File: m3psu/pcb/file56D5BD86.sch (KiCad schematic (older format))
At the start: 44 parts

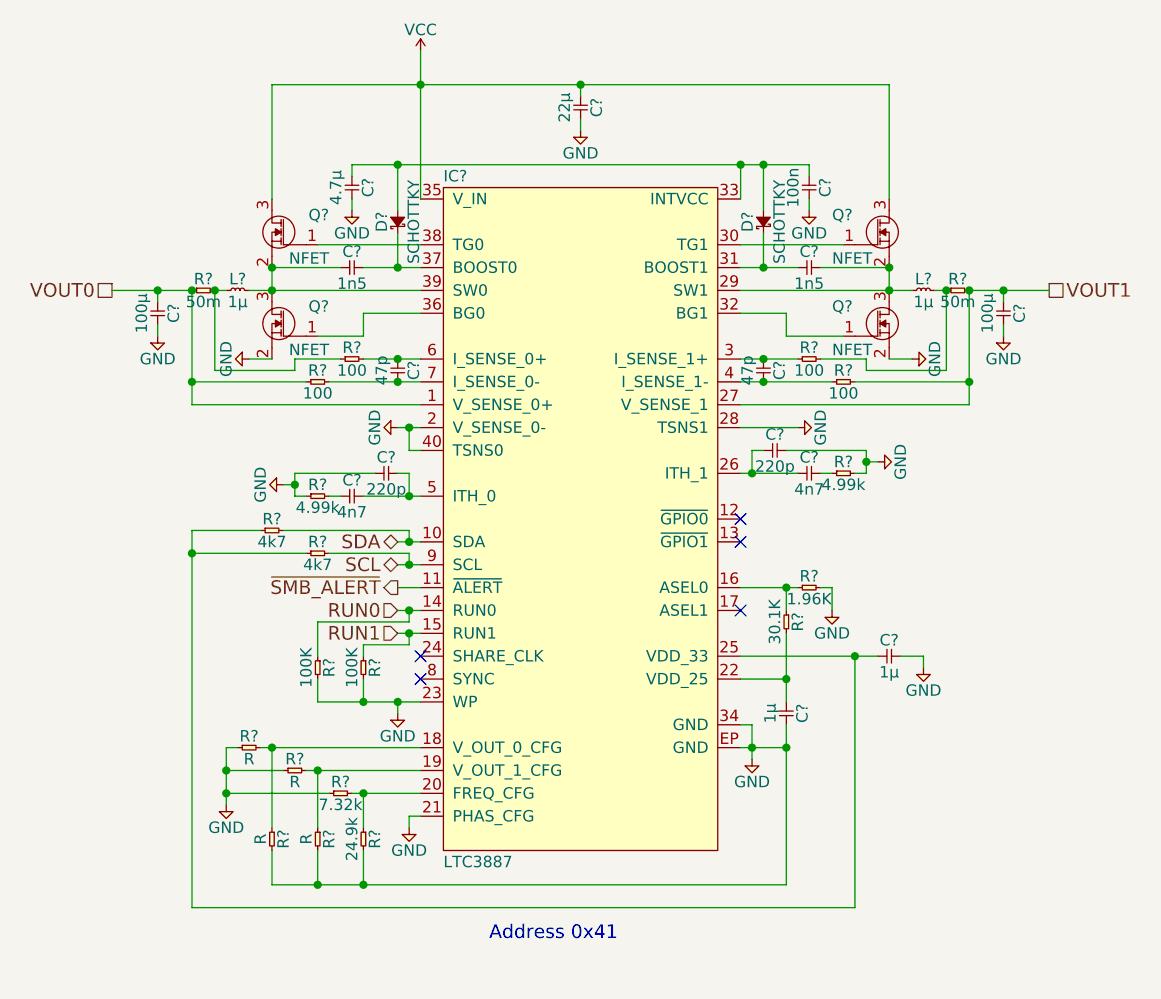
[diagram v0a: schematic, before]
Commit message: Add VOUT_CFG resistor values
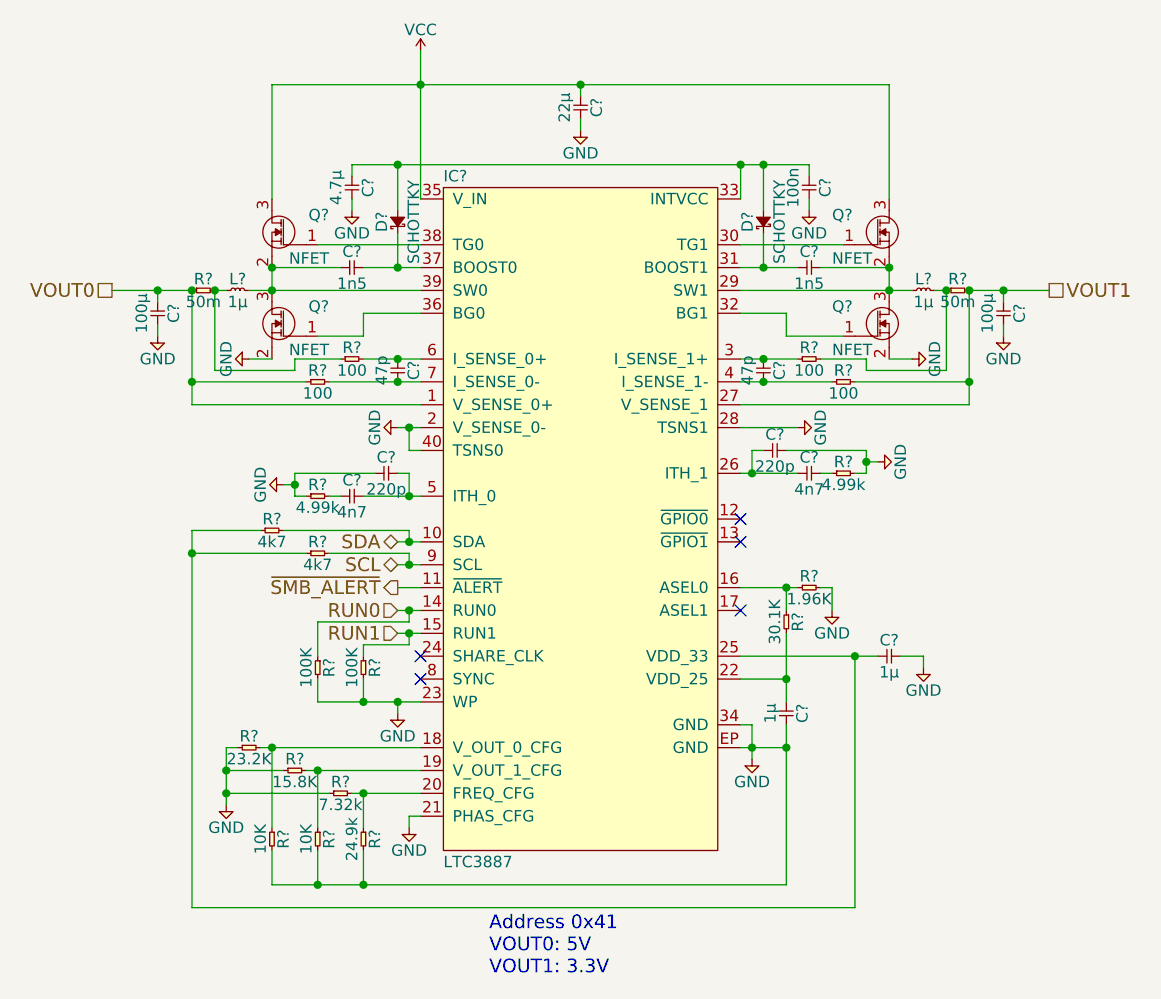
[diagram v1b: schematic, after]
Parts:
- R? (x2): value R -> 10K
- R?: value R -> 23.2K
- R?: value R -> 15.8K
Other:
- note added: "Address 0x41\nVOUT0: 5V\nVOUT1: 3.3V"
- note removed: "Address 0x41"
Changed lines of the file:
@@
 $Descr A4 11693 8268
 encoding utf-8
-Sheet 6 6
+Sheet 5 6
 Title ""
 Date ""
@@
 P 4700 5250
 F 0 "R?" H 4750 5300 50  0000 C CNN
-F 1 "R" H 4750 5200 50  0000 C CNN
+F 1 "10K" H 4750 5200 50  0000 C CNN
 F 2 "" H 4700 5250 50  0001 C CNN
 F 3 "" H 4700 5250 50  0001 C CNN
@@
 P 4500 5250
 F 0 "R?" H 4550 5300 50  0000 C CNN
-F 1 "R" H 4550 5200 50  0000 C CNN
+F 1 "10K" H 4550 5200 50  0000 C CNN
 F 2 "" H 4500 5250 50  0001 C CNN
 F 3 "" H 4500 5250 50  0001 C CNN
@@
 P 4350 4900
 F 0 "R?" H 4400 4950 50  0000 C CNN
-F 1 "R" H 4400 4850 50  0000 C CNN
+F 1 "23.2K" H 4400 4850 50  0000 C CNN
 F 2 "" H 4350 4900 50  0001 C CNN
 F 3 "" H 4350 4900 50  0001 C CNN
@@
 P 4550 5000
 F 0 "R?" H 4600 5050 50  0000 C CNN
-F 1 "R" H 4600 4950 50  0000 C CNN
+F 1 "15.8K" H 4600 4950 50  0000 C CNN
 F 2 "" H 4550 5000 50  0001 C CNN
 F 3 "" H 4550 5000 50  0001 C CNN
@@
 	4600 3800 4650 3800
 Wire Wire Line
-	4600 3700 4600 3750
-Wire Wire Line
-	4600 3750 4600 3800
+	4600 3700 4600 3800
 Wire Wire Line
 	4950 3700 4600 3700
@@
 Connection ~ 5100 3800
 Wire Wire Line
-	4900 3800 5100 3800
-Wire Wire Line
-	5100 3800 5150 3800
+	4900 3800 5150 3800
 Wire Wire Line
 	5100 3700 5100 3800
@@
 	7100 3700 7050 3700
 Wire Wire Line
-	7100 3600 7100 3650
-Wire Wire Line
-	7100 3650 7100 3700
+	7100 3600 7100 3700
 Wire Wire Line
 	6900 3700 6950 3700
@@
 	6600 3700 6600 3600
 Wire Wire Line
-	6550 3700 6600 3700
-Wire Wire Line
-	6600 3700 6800 3700
+	6550 3700 6800 3700
 Connection ~ 4150 4050
 Wire Wire Line
@@
 	5100 4100 5100 4050
 Wire Wire Line
-	5050 4100 5100 4100
-Wire Wire Line
-	5100 4100 5150 4100
+	5050 4100 5150 4100
 Connection ~ 5100 4000
 Wire Wire Line
-	5050 4000 5100 4000
-Wire Wire Line
-	5100 4000 5150 4000
-Wire Wire Line
-	4150 3950 4150 4050
-Wire Wire Line
-	4150 4050 4150 5600
-Wire Wire Line
-	5050 4300 5100 4300
-Wire Wire Line
-	5100 4300 5150 4300
-Wire Wire Line
-	5050 4400 5100 4400
-Wire Wire Line
-	5100 4400 5150 4400
+	5050 4000 5150 4000
+Wire Wire Line
+	4150 3950 4150 5600
+Wire Wire Line
+	5050 4300 5150 4300
+Wire Wire Line
+	5050 4400 5150 4400
 Wire Wire Line
 	6900 4200 6950 4200
@@
 	6750 4300 6750 4200
 Wire Wire Line
-	6550 4200 6750 4200
-Wire Wire Line
-	6750 4200 6800 4200
+	6550 4200 6800 4200
 Wire Wire Line
 	6950 4200 6950 4300
@@
 	5050 4700 5050 4750
 Wire Wire Line
-	4700 4700 4900 4700
-Wire Wire Line
-	4900 4700 5050 4700
-Wire Wire Line
-	5050 4700 5150 4700
+	4700 4700 5150 4700
 Wire Wire Line
 	4150 5600 7050 5600
@@
 	4550 5000 4300 5000
 Wire Wire Line
-	4300 4900 4300 5000
-Wire Wire Line
-	4300 5000 4300 5100
-Wire Wire Line
-	4300 5100 4300 5150
+	4300 4900 4300 5150
 Wire Wire Line
 	4350 4900 4300 4900
@@
 Connection ~ 4500 4900
 Wire Wire Line
-	4450 4900 4500 4900
-Wire Wire Line
-	4500 4900 5150 4900
+	4450 4900 5150 4900
 Wire Wire Line
 	4500 5250 4500 4900
 Wire Wire Line
-	4650 5000 4700 5000
-Wire Wire Line
-	4700 5000 5150 5000
+	4650 5000 5150 5000
 Wire Wire Line
 	4700 5250 4700 5000
 Wire Wire Line
-	4850 5100 4900 5100
-Wire Wire Line
-	4900 5100 5150 5100
+	4850 5100 5150 5100
 Wire Wire Line
 	4900 5100 4900 5250
@@
 Connection ~ 6750 4900
 Wire Wire Line
-	6750 5500 4900 5500
-Wire Wire Line
-	4900 5500 4700 5500
-Wire Wire Line
-	4700 5500 4500 5500
+	6750 5500 4500 5500
 Wire Wire Line
 	7250 4500 7350 4500
 Wire Wire Line
-	6550 4900 6600 4900
-Wire Wire Line
-	6600 4900 6750 4900
+	6550 4900 6750 4900
 Wire Wire Line
 	7350 4500 7350 4550
@@
 	6850 2350 6850 2400
 Wire Wire Line
-	4850 2350 5050 2350
-Wire Wire Line
-	5050 2350 6550 2350
-Wire Wire Line
-	6550 2350 6650 2350
-Wire Wire Line
-	6650 2350 6850 2350
+	4850 2350 6850 2350
 Wire Wire Line
 	4850 2400 4850 2350
@@
 	4400 3200 4500 3200
 Wire Wire Line
-	5050 3500 5100 3500
-Wire Wire Line
-	5100 3500 5150 3500
-Wire Wire Line
-	6750 4800 6750 4900
-Wire Wire Line
-	6750 4900 6750 5500
-Wire Wire Line
-	6550 4500 7050 4500
-Wire Wire Line
-	7050 4500 7150 4500
-Wire Wire Line
-	6750 4400 6750 4600
-Wire Wire Line
-	6750 4600 6750 4700
+	5050 3500 5150 3500
+Wire Wire Line
+	6750 4800 6750 5500
+Wire Wire Line
+	6550 4500 7150 4500
+Wire Wire Line
+	6750 4400 6750 4700
 Wire Wire Line
 	6550 4600 6750 4600
 Connection ~ 6600 4900
 Wire Wire Line
-	6600 4800 6600 4900
-Wire Wire Line
-	6600 4900 6600 4950
+	6600 4800 6600 4950
 Wire Wire Line
 	6550 4800 6600 4800
@@
 Connection ~ 5050 3200
 Wire Wire Line
-	4900 3200 5050 3200
-Wire Wire Line
-	5050 3200 5150 3200
-Wire Wire Line
-	4750 3300 5050 3300
-Wire Wire Line
-	5050 3300 5150 3300
+	4900 3200 5150 3200
+Wire Wire Line
+	4750 3300 5150 3300
 Wire Wire Line
 	4150 3300 4650 3300
@@
 Connection ~ 4150 2900
 Wire Wire Line
-	4150 2900 4150 3300
-Wire Wire Line
-	4150 3300 4150 3400
+	4150 2900 4150 3400
 Connection ~ 4250 2900
 Wire Wire Line
@@
 	4000 3050 4000 3100
 Wire Wire Line
-	3800 2900 4000 2900
-Wire Wire Line
-	4000 2900 4150 2900
+	3800 2900 4150 2900
 Wire Wire Line
 	4000 2950 4000 2900
@@
 	7700 2950 7700 2900
 Wire Wire Line
-	7550 2900 7700 2900
-Wire Wire Line
-	7700 2900 7900 2900
+	7550 2900 7900 2900
 Connection ~ 7550 3300
 Wire Wire Line
@@
 Connection ~ 7450 2900
 Wire Wire Line
-	7550 2900 7550 3300
-Wire Wire Line
-	7550 3300 7550 3400
+	7550 2900 7550 3400
 Wire Wire Line
 	7050 3300 7550 3300
 Wire Wire Line
-	6550 3200 6650 3200
-Wire Wire Line
-	6650 3200 6800 3200
+	6550 3200 6800 3200
 Wire Wire Line
 	7100 3200 6900 3200
 Wire Wire Line
-	6550 3300 6650 3300
-Wire Wire Line
-	6650 3300 6950 3300
+	6550 3300 6950 3300
 Wire Wire Line
 	7100 3250 7100 3200
@@
 Connection ~ 4500 2900
 Wire Wire Line
-	4400 2900 4500 2900
-Wire Wire Line
-	4500 2900 5150 2900
+	4400 2900 5150 2900
 Wire Wire Line
 	4500 2800 4500 2900
@@
 	4700 2700 5150 2700
 Wire Wire Line
-	4900 2800 5050 2800
-Wire Wire Line
-	5050 2800 5150 2800
+	4900 2800 5150 2800
 Connection ~ 5850 2000
 Wire Wire Line
@@
 Connection ~ 5150 2000
 Wire Wire Line
-	4500 2000 5150 2000
-Wire Wire Line
-	5150 2000 5850 2000
-Wire Wire Line
-	5850 2000 7200 2000
+	4500 2000 7200 2000
 Wire Wire Line
 	7200 2000 7200 2500
 Wire Wire Line
-	5150 1850 5150 2000
-Wire Wire Line
-	5150 2000 5150 2500
+	5150 1850 5150 2500
 Connection ~ 7200 2800
 Wire Wire Line
@@
 Connection ~ 7200 2900
 Wire Wire Line
-	6550 2900 7200 2900
-Wire Wire Line
-	7200 2900 7300 2900
+	6550 2900 7300 2900
 Wire Wire Line
 	6900 2800 7200 2800
 Wire Wire Line
-	6550 2800 6650 2800
-Wire Wire Line
-	6650 2800 6800 2800
+	6550 2800 6800 2800
 Wire Wire Line
 	6750 3100 7000 3100
@@
 Text HLabel 5050 4200 0    60   Output ~ 0
 ~SMB_ALERT
-Text Notes 5450 5750 0    60   ~ 0
-Address 0x41
-$Comp
-L R R?
+Text Notes 5450 5900 0    60   ~ 0
+Address 0x41\nVOUT0: 5V\nVOUT1: 3.3V
+$Comp
+L R R?

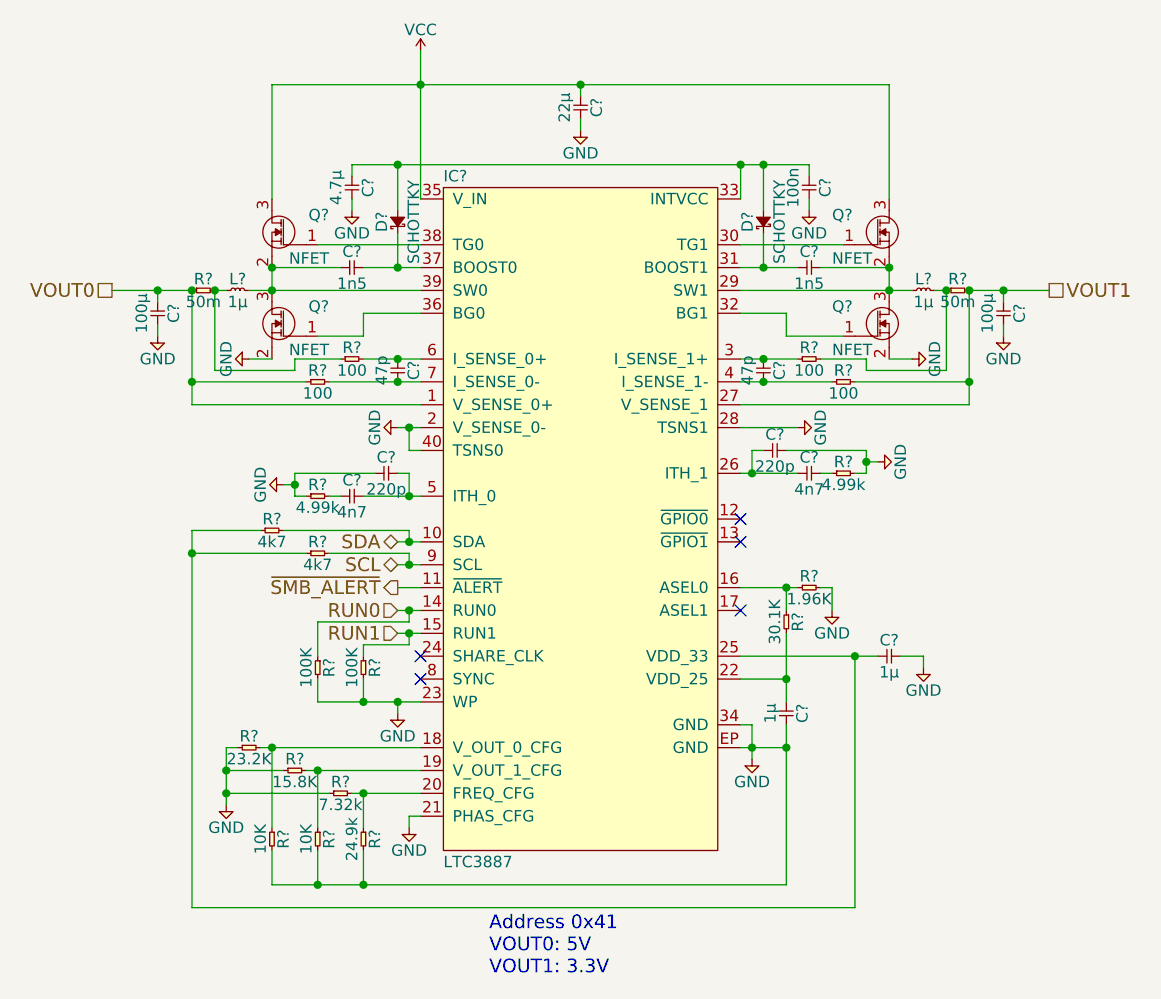
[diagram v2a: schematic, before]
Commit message: Finished passives for Li-ion Charger. Tweaked and cleaned up values in DC/DC Converter.
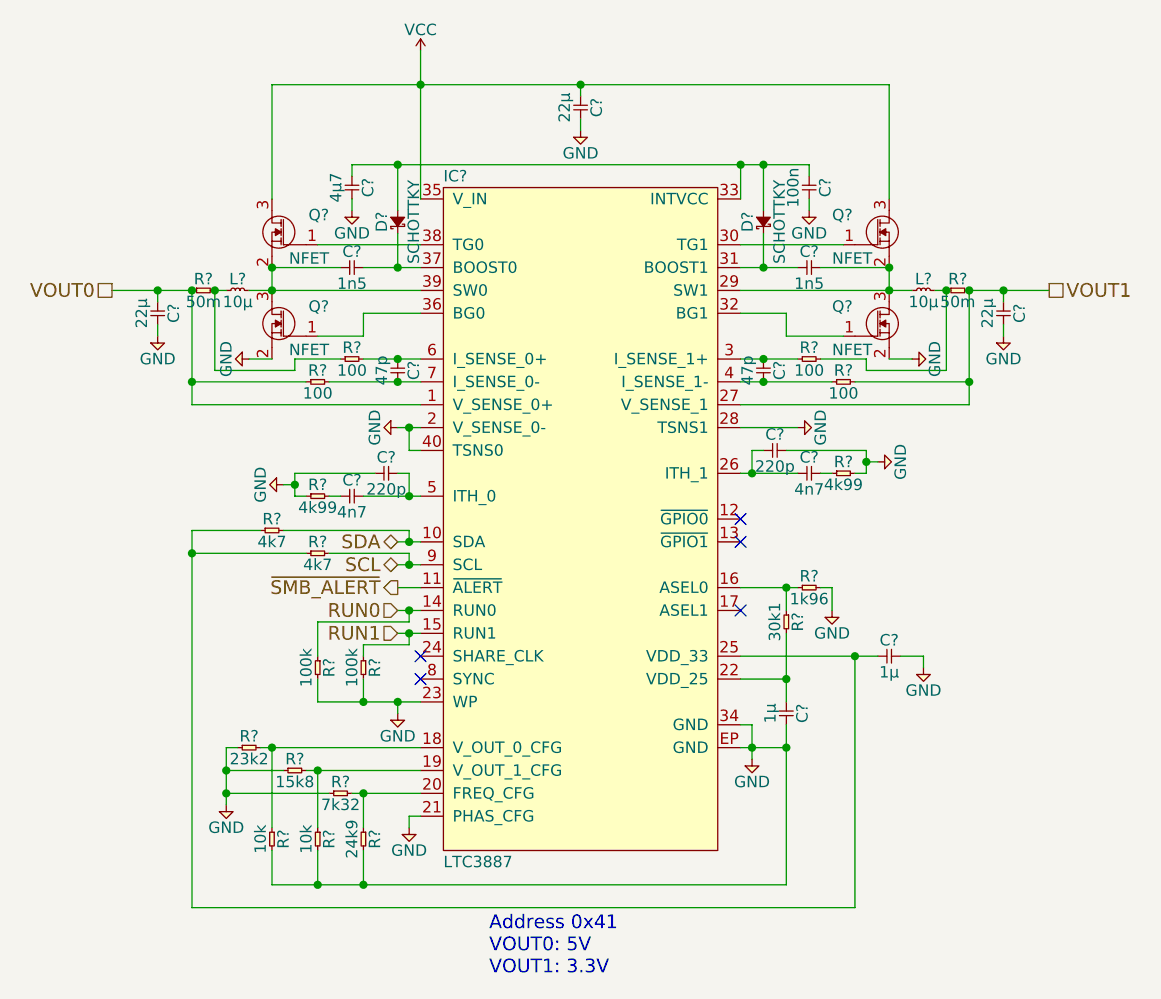
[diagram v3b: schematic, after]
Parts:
- C?: value 4.7µ -> 4µ7
- C? (x2): value 100µ -> 22µ; Farnell 1735535 -> 2494232
- L? (x2): value 1µ -> 10µ; Farnell 2292535 -> 2292532
- R?: value 24.9k -> 24k9
- R? (x2): value 10K -> 10k
- R?: value 23.2K -> 23k2
- R?: value 15.8K -> 15k8
- R?: value 7.32k -> 7k32
- R?: value 1.96K -> 1k96
- R?: value 30.1K -> 30k1
- R? (x2): value 4.99k -> 4k99
- R? (x2): value 100K -> 100k
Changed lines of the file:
@@
 P 7300 2900
 F 0 "L?" H 7350 2950 50  0000 C CNN
-F 1 "1µ" H 7350 2850 50  0000 C CNN
+F 1 "10µ" H 7350 2850 50  0000 C CNN
 F 2 "" H 7300 2900 50  0001 C CNN
 F 3 "" H 7300 2900 50  0001 C CNN
-F 4 "2292535" H 7300 2900 60  0001 C CNN "Farnell"
+F 4 "2292532" H 7300 2900 60  0001 C CNN "Farnell"
 	1    7300 2900
 	1    0    0    -1
@@
 P 4300 2900
 F 0 "L?" H 4350 2950 50  0000 C CNN
-F 1 "1µ" H 4350 2850 50  0000 C CNN
+F 1 "10µ" H 4350 2850 50  0000 C CNN
 F 2 "" H 4300 2900 50  0001 C CNN
 F 3 "" H 4300 2900 50  0001 C CNN
-F 4 "2292535" H 4300 2900 60  0001 C CNN "Farnell"
+F 4 "2292532" H 4300 2900 60  0001 C CNN "Farnell"
 	1    4300 2900
 	1    0    0    -1
@@
 P 4850 2400
 F 0 "C?" H 4900 2470 50  0000 C CNN
-F 1 "4.7µ" H 4900 2330 50  0000 C CNN
+F 1 "4µ7" H 4900 2330 50  0000 C CNN
 F 2 "" H 4850 2400 50  0001 C CNN
 F 3 "" H 4850 2400 50  0001 C CNN
@@
 P 7700 2950
 F 0 "C?" H 7750 3020 50  0000 C CNN
-F 1 "100µ" H 7750 2880 50  0000 C CNN
+F 1 "22µ" H 7750 2880 50  0000 C CNN
 F 2 "" H 7700 2950 50  0001 C CNN
 F 3 "" H 7700 2950 50  0001 C CNN
-F 4 "1735535" H 7700 2950 60  0001 C CNN "Farnell"
+F 4 "2494232" H 7700 2950 60  0001 C CNN "Farnell"
 	1    7700 2950
 	0    1    1    0
@@
 P 4000 2950
 F 0 "C?" H 4050 3020 50  0000 C CNN
-F 1 "100µ" H 4050 2880 50  0000 C CNN
+F 1 "22µ" H 4050 2880 50  0000 C CNN
 F 2 "" H 4000 2950 50  0001 C CNN
 F 3 "" H 4000 2950 50  0001 C CNN
-F 4 "1735535" H 4000 2950 60  0001 C CNN "Farnell"
+F 4 "2494232" H 4000 2950 60  0001 C CNN "Farnell"
 	1    4000 2950
 	0    1    1    0
@@
 P 4900 5250
 F 0 "R?" H 4950 5300 50  0000 C CNN
-F 1 "24.9k" H 4950 5200 50  0000 C CNN
+F 1 "24k9" H 4950 5200 50  0000 C CNN
 F 2 "" H 4900 5250 50  0001 C CNN
 F 3 "" H 4900 5250 50  0001 C CNN
@@
 P 4700 5250
 F 0 "R?" H 4750 5300 50  0000 C CNN
-F 1 "10K" H 4750 5200 50  0000 C CNN
+F 1 "10k" H 4750 5200 50  0000 C CNN
 F 2 "" H 4700 5250 50  0001 C CNN
 F 3 "" H 4700 5250 50  0001 C CNN
@@
 P 4500 5250
 F 0 "R?" H 4550 5300 50  0000 C CNN
-F 1 "10K" H 4550 5200 50  0000 C CNN
+F 1 "10k" H 4550 5200 50  0000 C CNN
 F 2 "" H 4500 5250 50  0001 C CNN
 F 3 "" H 4500 5250 50  0001 C CNN
@@
 P 4350 4900
 F 0 "R?" H 4400 4950 50  0000 C CNN
-F 1 "23.2K" H 4400 4850 50  0000 C CNN
+F 1 "23k2" H 4400 4850 50  0000 C CNN
 F 2 "" H 4350 4900 50  0001 C CNN
 F 3 "" H 4350 4900 50  0001 C CNN
@@
 P 4550 5000
 F 0 "R?" H 4600 5050 50  0000 C CNN
-F 1 "15.8K" H 4600 4950 50  0000 C CNN
+F 1 "15k8" H 4600 4950 50  0000 C CNN
 F 2 "" H 4550 5000 50  0001 C CNN
 F 3 "" H 4550 5000 50  0001 C CNN
@@
 P 4750 5100
 F 0 "R?" H 4800 5150 50  0000 C CNN
-F 1 "7.32k" H 4800 5050 50  0000 C CNN
+F 1 "7k32" H 4800 5050 50  0000 C CNN
 F 2 "" H 4750 5100 50  0001 C CNN
 F 3 "" H 4750 5100 50  0001 C CNN
@@
 P 6800 4200
 F 0 "R?" H 6850 4250 50  0000 C CNN
-F 1 "1.96K" H 6850 4150 50  0000 C CNN
+F 1 "1k96" H 6850 4150 50  0000 C CNN
 F 2 "" H 6800 4200 50  0001 C CNN
 F 3 "" H 6800 4200 50  0001 C CNN
@@
 P 6750 4300
 F 0 "R?" H 6800 4350 50  0000 C CNN
-F 1 "30.1K" H 6800 4250 50  0000 C CNN
+F 1 "30k1" H 6800 4250 50  0000 C CNN
 F 2 "" H 6750 4300 50  0001 C CNN
 F 3 "" H 6750 4300 50  0001 C CNN
@@
 P 6950 3700
 F 0 "R?" H 7000 3750 50  0000 C CNN
-F 1 "4.99k" H 7000 3650 50  0000 C CNN
+F 1 "4k99" H 7000 3650 50  0000 C CNN
 F 2 "" H 6950 3700 50  0001 C CNN
 F 3 "" H 6950 3700 50  0001 C CNN
@@
 P 4650 3800
 F 0 "R?" H 4700 3850 50  0000 C CNN
-F 1 "4.99k" H 4700 3750 50  0000 C CNN
+F 1 "4k99" H 4700 3750 50  0000 C CNN
 F 2 "" H 4650 3800 50  0001 C CNN
 F 3 "" H 4650 3800 50  0001 C CNN
@@
 P 4900 4500
 F 0 "R?" H 4950 4550 50  0000 C CNN
-F 1 "100K" H 4950 4450 50  0000 C CNN
+F 1 "100k" H 4950 4450 50  0000 C CNN
 F 2 "" H 4900 4500 50  0001 C CNN
 F 3 "" H 4900 4500 50  0001 C CNN
@@
 P 4700 4500
 F 0 "R?" H 4750 4550 50  0000 C CNN
-F 1 "100K" H 4750 4450 50  0000 C CNN
+F 1 "100k" H 4750 4450 50  0000 C CNN
 F 2 "" H 4700 4500 50  0001 C CNN
 F 3 "" H 4700 4500 50  0001 C CNN

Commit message: Linked the footprints to some parts. Cleaned up a little more of DC/DC Converter.
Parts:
- C?: footprint (none) -> agg:0603
- C?: Farnell (none) -> 2494232
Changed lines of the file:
@@
 F 0 "C?" H 4900 2470 50  0000 C CNN
 F 1 "4µ7" H 4900 2330 50  0000 C CNN
-F 2 "" H 4850 2400 50  0001 C CNN
+F 2 "agg:0603" H 4850 2400 50  0001 C CNN
 F 3 "" H 4850 2400 50  0001 C CNN
 	1    4850 2400
@@
 F 2 "" H 5850 2050 50  0001 C CNN
 F 3 "" H 5850 2050 50  0001 C CNN
+F 4 "2494232" H 5850 2050 60  0001 C CNN "Farnell"
 	1    5850 2050
 	0    1    1    0
